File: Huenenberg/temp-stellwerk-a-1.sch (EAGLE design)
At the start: 117 parts, among them Q1 BSS123, Q10 BSS84, Q11 BSS123, Q12 BSS84, Q13 BSS123, Q14 BSS84, Q15 BSS123, Q16 BSS84, Q17 BSS123, Q18 BSS84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

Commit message: Updates some of the values of the parts.
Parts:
- DW1N, DW1R, DW2AN, DW2AR, DW7AR: device led:LEDCHIP-LED0805 -> led:LEDCHIP-LED0603
- DW7AN: device led:LEDCHIP-LED0805 -> led:LEDCHIPLED_0603
- W1011, W34, W56, W89: value W1 -> XOVER

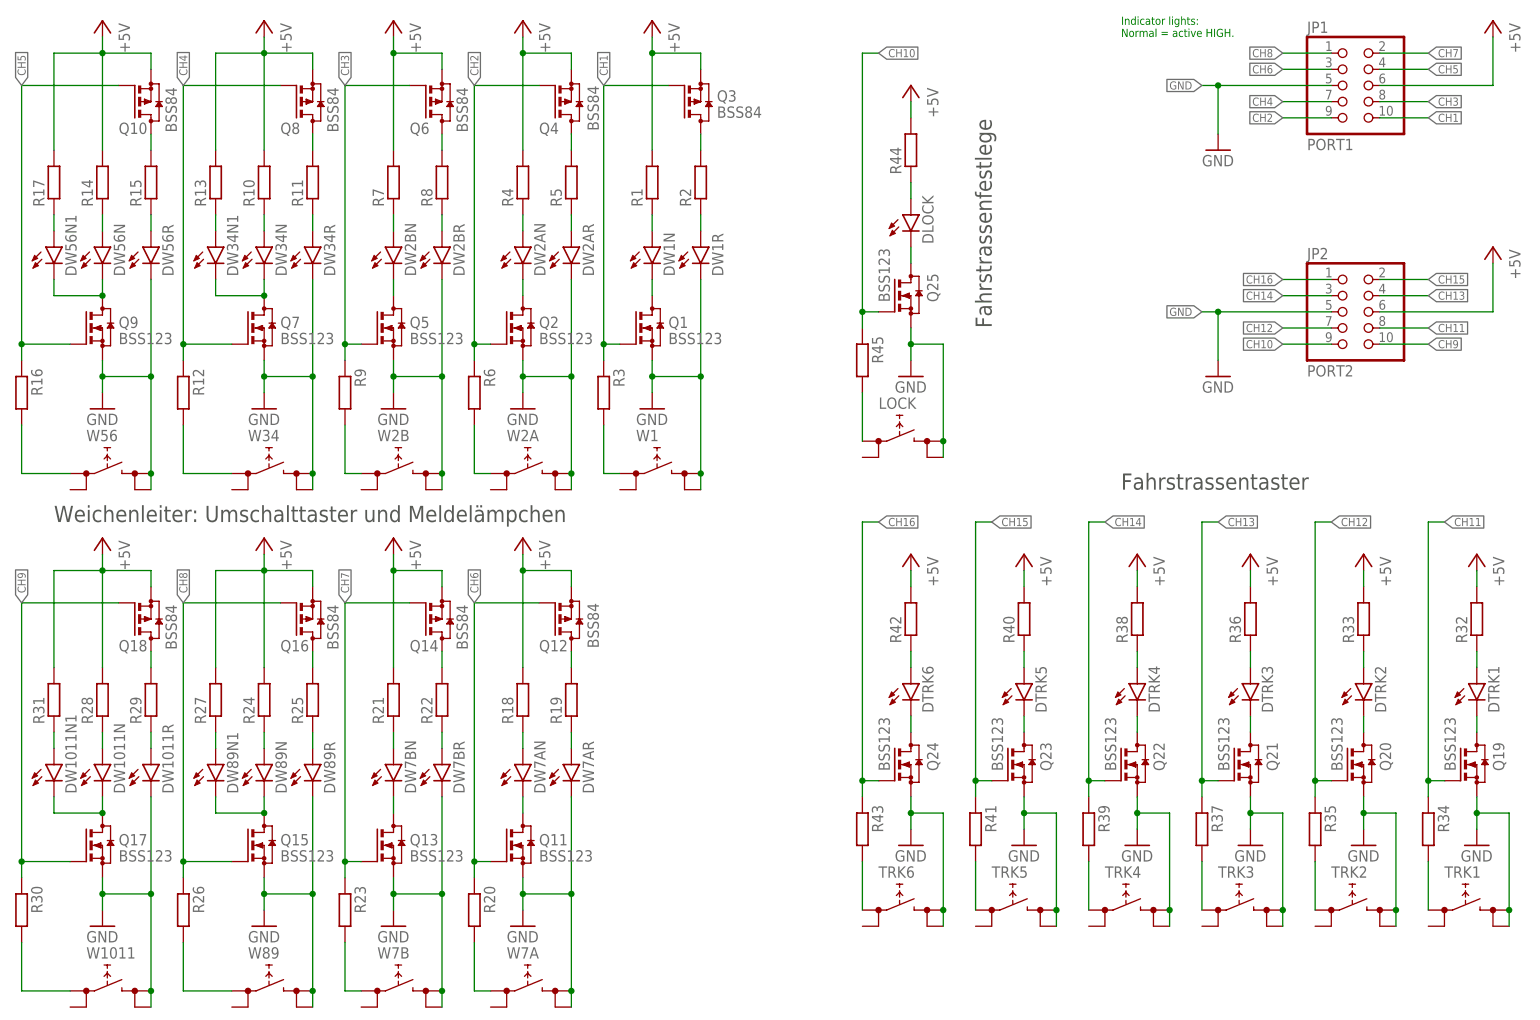
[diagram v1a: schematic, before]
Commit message: Updates names of all buttons.
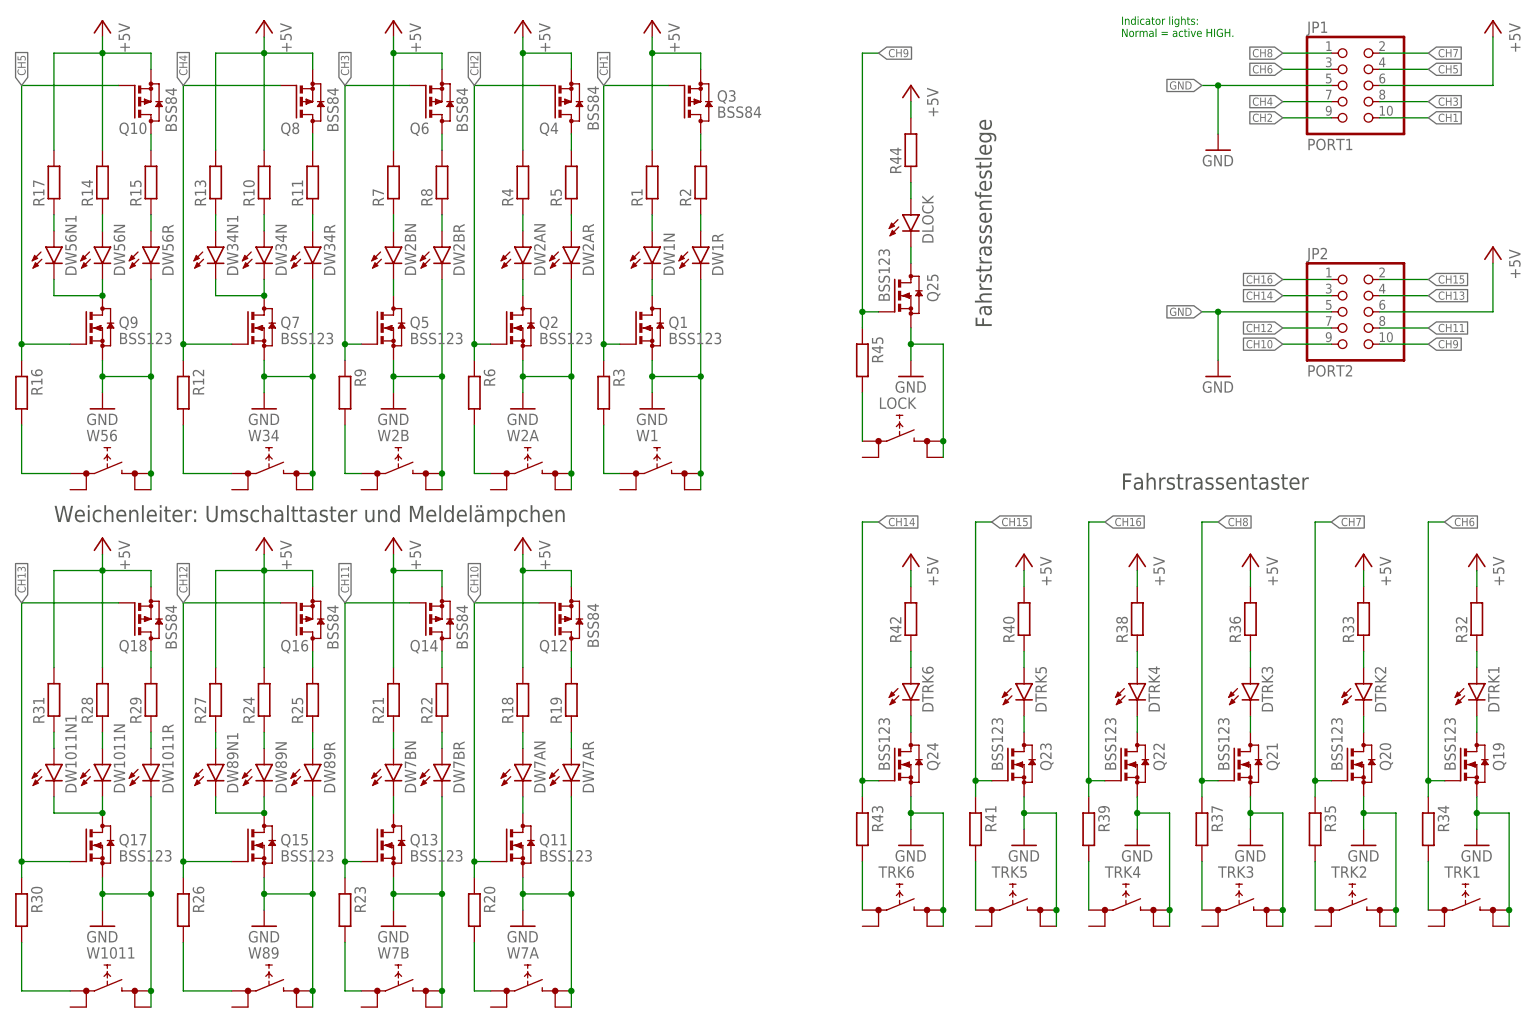
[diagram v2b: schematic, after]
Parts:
- LOCK: value W2 -> LOCK
- TRK1, TRK2, TRK3, TRK4, TRK5, TRK6, W2A, W7A: value W2 -> TACTSW-6X6S
- W2B, W7B: value W1 -> TACTSW-6X6S
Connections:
- net CH10: now also Q11.G, Q12.G, R20.1; no longer Q25.G, R45.1
- net CH11: now also Q13.G, Q14.G, R23.1; no longer Q19.G, R34.1
- net CH12: now also Q15.G, Q16.G, R26.1; no longer Q20.G, R35.1
- net CH13: now also Q17.G, Q18.G, R30.1; no longer Q21.G, R37.1
- net CH14: now also Q24.G, R43.1; no longer Q22.G, R39.1
- net CH16: now also Q22.G, R39.1; no longer Q24.G, R43.1
- net CH6: now also Q19.G, R34.1; no longer Q11.G, Q12.G, R20.1
- net CH7: now also Q20.G, R35.1; no longer Q13.G, Q14.G, R23.1
- net CH8: now also Q21.G, R37.1; no longer Q15.G, Q16.G, R26.1
- net CH9: now also Q25.G, R45.1; no longer Q17.G, Q18.G, R30.1

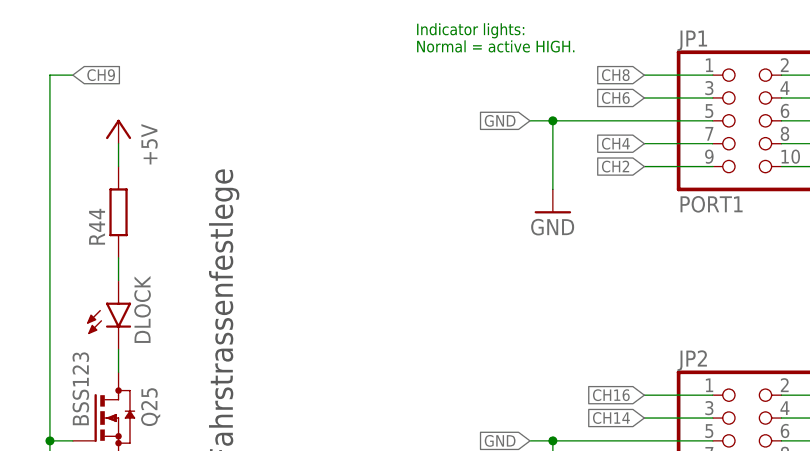
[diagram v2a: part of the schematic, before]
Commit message: Lays out all SMD parts on the bottom side.
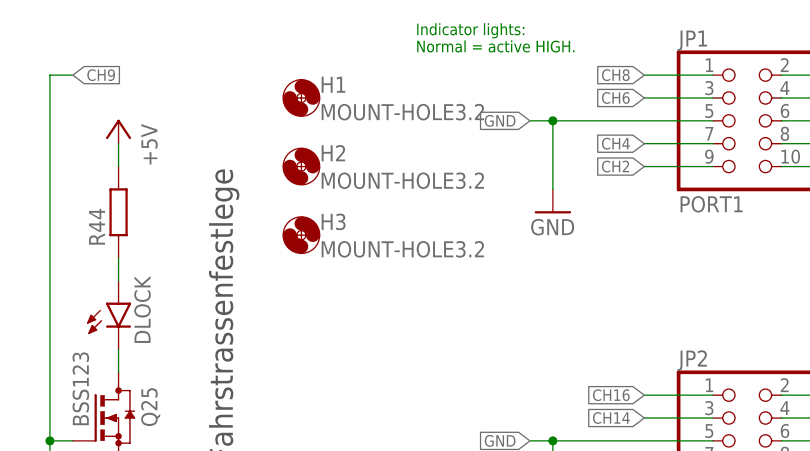
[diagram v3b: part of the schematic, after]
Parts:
- added H1, H2, H3: MOUNT-HOLE3.2, holes:MOUNT-HOLE3.2
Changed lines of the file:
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@@
 <part name="P+17" library="supply1" library_urn="urn:adsk.eagle:library:371" deviceset="+5V" device=""/>
 <part name="R45" library="rcl" library_urn="urn:adsk.eagle:library:334" deviceset="R-EU_" device="R0805" package3d_urn="urn:adsk.eagle:package:23553/2"/>
+<part name="H1" library="holes" library_urn="urn:adsk.eagle:library:237" deviceset="MOUNT-HOLE" device="3.2" package3d_urn="urn:adsk.eagle:package:14275/1"/>
+<part name="H2" library="holes" library_urn="urn:adsk.eagle:library:237" deviceset="MOUNT-HOLE" device="3.2" package3d_urn="urn:adsk.eagle:package:14275/1"/>
+<part name="H3" library="holes" library_urn="urn:adsk.eagle:library:237" deviceset="MOUNT-HOLE" device="3.2" package3d_urn="urn:adsk.eagle:package:14275/1"/>
 </parts>
 <sheets>
@@
 <attribute name="VALUE" x="128.778" y="105.41" size="1.778" layer="96" rot="R270"/>
 </instance>
+<instance part="H1" gate="G$1" x="160.02" y="147.32" smashed="yes">
+<attribute name="NAME" x="162.052" y="147.9042" size="1.778" layer="95"/>
+<attribute name="VALUE" x="162.052" y="144.8562" size="1.778" layer="96"/>
+</instance>
+<instance part="H2" gate="G$1" x="160.02" y="139.7" smashed="yes">
+<attribute name="NAME" x="162.052" y="140.2842" size="1.778" layer="95"/>
+<attribute name="VALUE" x="162.052" y="137.2362" size="1.778" layer="96"/>
+</instance>
+<instance part="H3" gate="G$1" x="160.02" y="132.08" smashed="yes">
+<attribute name="NAME" x="162.052" y="132.6642" size="1.778" layer="95"/>
+<attribute name="VALUE" x="162.052" y="129.6162" size="1.778" layer="96"/>
+</instance>
 </instances>
